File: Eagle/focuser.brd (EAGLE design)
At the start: 52 x 110.2 mm, 50 parts, among them IC1 78xx, J1 J5MM, J10 J5MM, J2 J7MM, J3 J7MM, J4 J5MM, J5 J7MM, J6 J12MM, J7 J7MM, J8 J7MM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

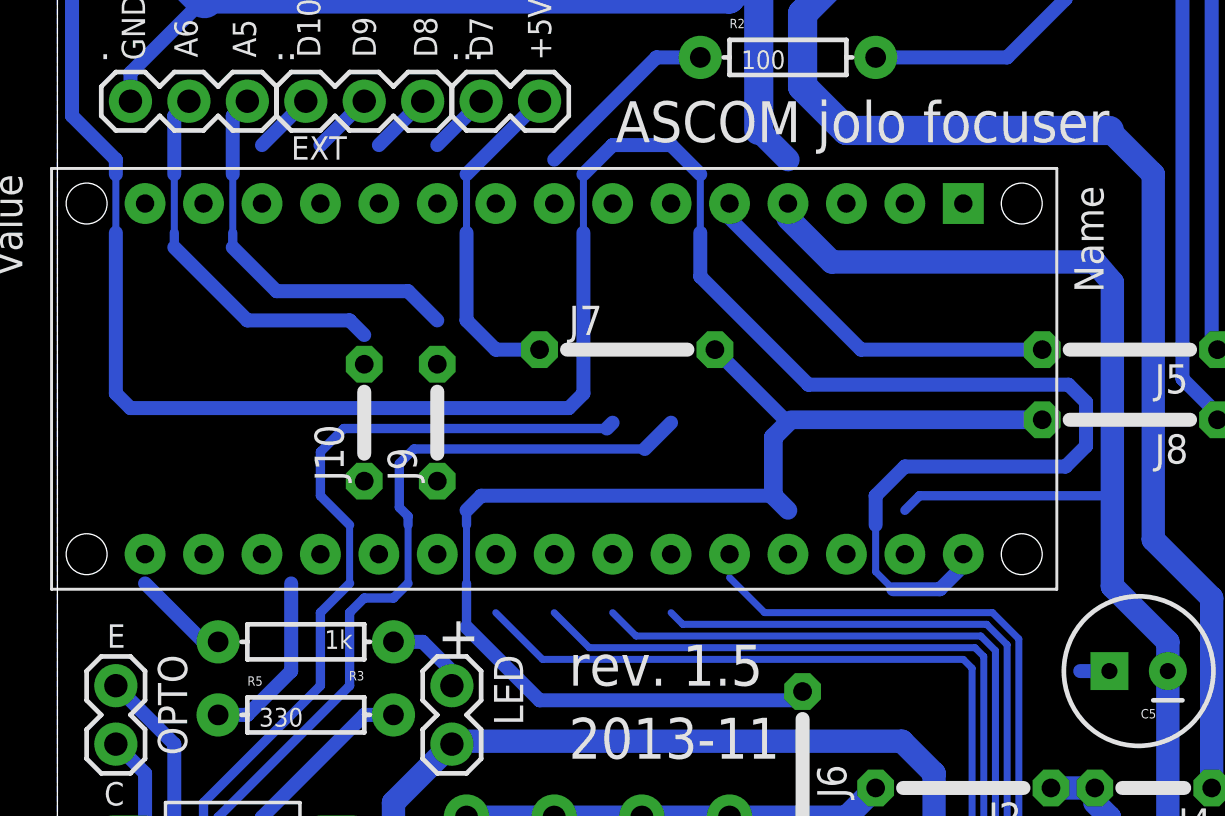
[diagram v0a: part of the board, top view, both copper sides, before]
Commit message: PCB fix for 1.6
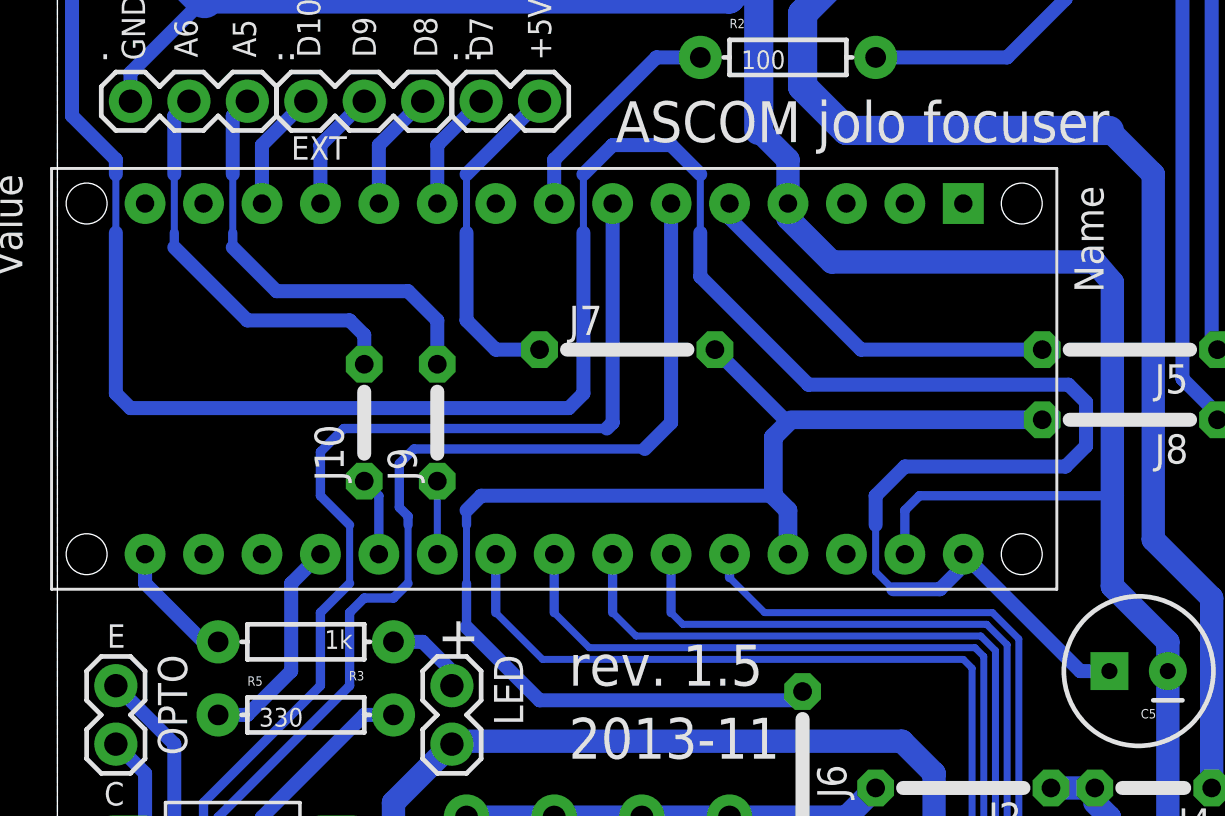
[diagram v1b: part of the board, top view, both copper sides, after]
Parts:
- NANO: value ARDUINONANO -> MMduino
- renumbered U$1 to NANO
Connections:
- removed net N$4 (its old number): NANO.A6, U1.10
- removed net N$41: J9.2, NANO.A0
- new net N$13: NANO.A1, U1.10
- new net N$25: J10.1, NANO.A6
- net N$12: now also J9.1, NANO.A5; no longer J10.2, NANO.A1
- net N$3: now also NANO.A0; no longer NANO.D6
- net N$31: now also J10.2; no longer J10.1
- net N$40: now also J9.2; no longer J9.1
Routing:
- net N$13: track 0.00 -> 41.8 mm
- net N$4 (its old number): track 39.2 -> 0.00 mm
- net N$24: track 100.7 -> 110.2 mm
- net N$18: track 80.0 -> 89.6 mm
- net N$9: track 146.6 -> 154.2 mm
- net GND: track 374.5 -> 378.9 mm
- net N$25: track 0.00 -> 3.44 mm
- net N$12: track 0.00 -> 3.17 mm
- net N$5: track 39.5 -> 42.1 mm
- net N$4: track 38.4 -> 40.9 mm
- net N$15: track 43.8 -> 46.4 mm
- net N$34: track 2.69 -> 5.23 mm
- net N$33: track 2.69 -> 5.23 mm
- net N$32: track 2.69 -> 5.23 mm
- net N$8: track 2.69 -> 5.23 mm
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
